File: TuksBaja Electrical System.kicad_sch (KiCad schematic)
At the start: 0 parts

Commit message: added two resistors to schematic
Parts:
- added R1, R2: R, symbol Device:R
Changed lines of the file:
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@@
 	(generator_version "9.0")
 	(paper "A4")
+	(symbol
+		(lib_id "Device:R")
+		(at 30.48 83.82 0)
+		(unit 1)
+		(exclude_from_sim no)
+		(in_bom yes)
+		(on_board yes)
+		(dnp no)
+		(fields_autoplaced yes)
+		(property "Reference" "R1"
+			(at 33.02 82.5499 0)
+			(effects
+				(font
+					(size 1.27 1.27)
+				)
+				(justify left)
+			)
+		)
+		(property "Value" "R"
+			(at 33.02 85.0899 0)
+			(effects
+				(font
+					(size 1.27 1.27)
+				)
+				(justify left)
+			)
+		)
+		(property "Footprint" ""
+			(at 28.702 83.82 90)
+			(effects
+				(font
+					(size 1.27 1.27)
+				)
+				(hide yes)
+			)
+		)
+		(property "Datasheet" "~"
+			(at 30.48 83.82 0)
+			(effects
+				(font
+					(size 1.27 1.27)
+				)
+				(hide yes)
+			)
+		)
+		(property "Description" "Resistor"
+			(at 30.48 83.82 0)
+			(effects
+				(font
+					(size 1.27 1.27)
+				)
+				(hide yes)
+			)
+		)
+		(pin "1"
+		)
+		(pin "2"
+		)
+		(instances
+			(project ""
+				(path "/32101482-20ad-4a29-9fb3-a9077501af62"
+					(reference "R1")
+					(unit 1)
+				)
+			)
+		)
+	)
+	(symbol
+		(lib_id "Device:R")
+		(at 30.48 105.41 0)
+		(unit 1)
+		(exclude_from_sim no)
+		(in_bom yes)
+		(on_board yes)
+		(dnp no)
+		(fields_autoplaced yes)
+		(property "Reference" "R2"
+			(at 33.02 104.1399 0)
+			(effects
+				(font
+					(size 1.27 1.27)
+				)
+				(justify left)
+			)
+		)
+		(property "Value" "R"
+			(at 33.02 106.6799 0)
+			(effects
+				(font
+					(size 1.27 1.27)
+				)
+				(justify left)
+			)
+		)
+		(property "Footprint" ""
+			(at 28.702 105.41 90)
+			(effects
+				(font
+					(size 1.27 1.27)
+				)
+				(hide yes)
+			)
+		)
+		(property "Datasheet" "~"
+			(at 30.48 105.41 0)
+			(effects
+				(font
+					(size 1.27 1.27)
+				)
+				(hide yes)
+			)
+		)
+		(property "Description" "Resistor"
+			(at 30.48 105.41 0)
+			(effects
+				(font
+					(size 1.27 1.27)
+				)
+				(hide yes)
+			)
+		)
+		(pin "2"
+		)
+		(pin "1"
+		)
+		(instances
+			(project ""
+				(path "/32101482-20ad-4a29-9fb3-a9077501af62"
+					(reference "R2")
+					(unit 1)
+				)
+			)
+		)
+	)
 	(sheet_instances
 		(path "/"

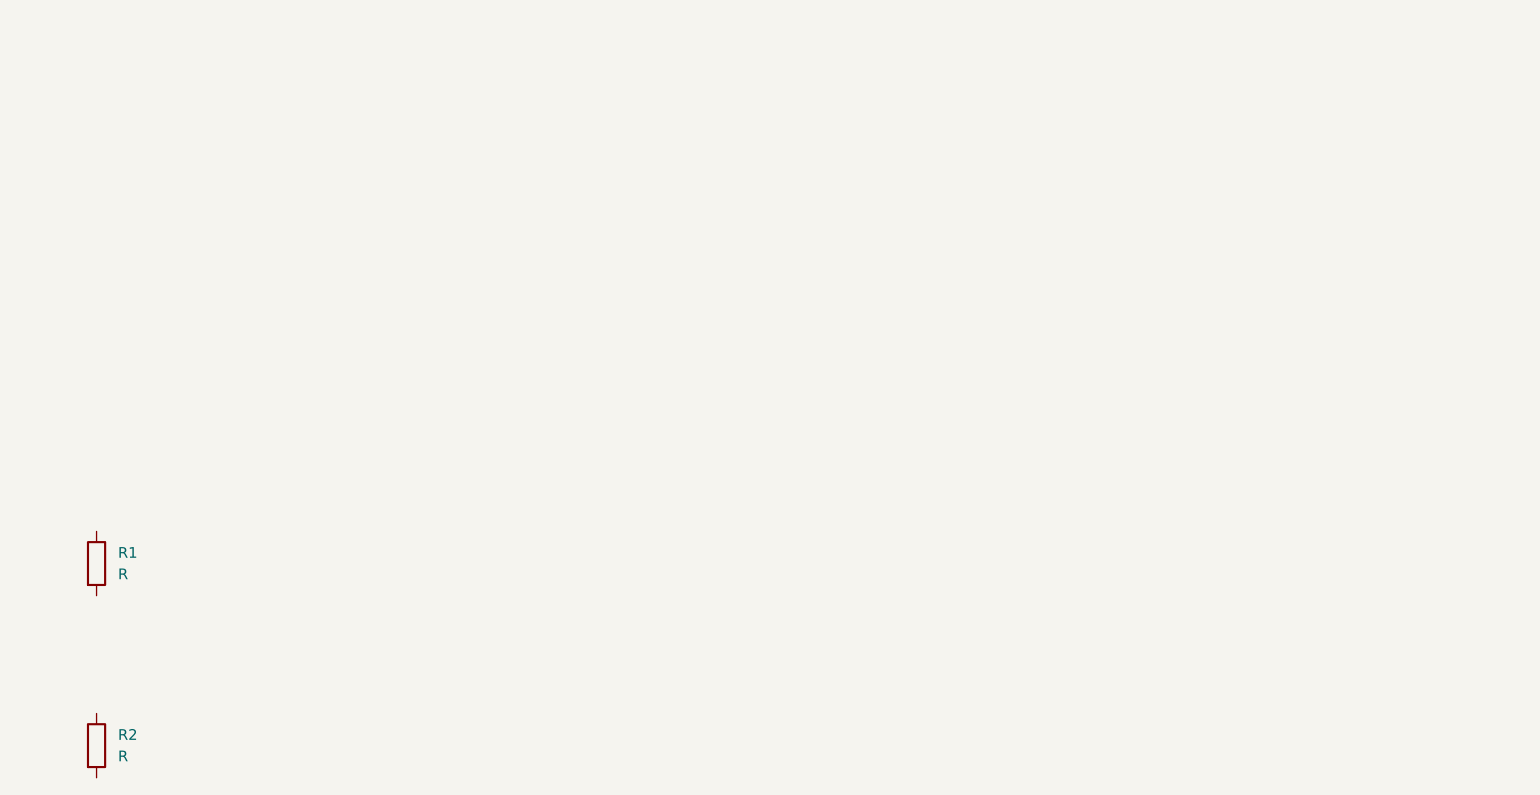
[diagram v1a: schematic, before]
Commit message: added arduino, buck converter, and battery
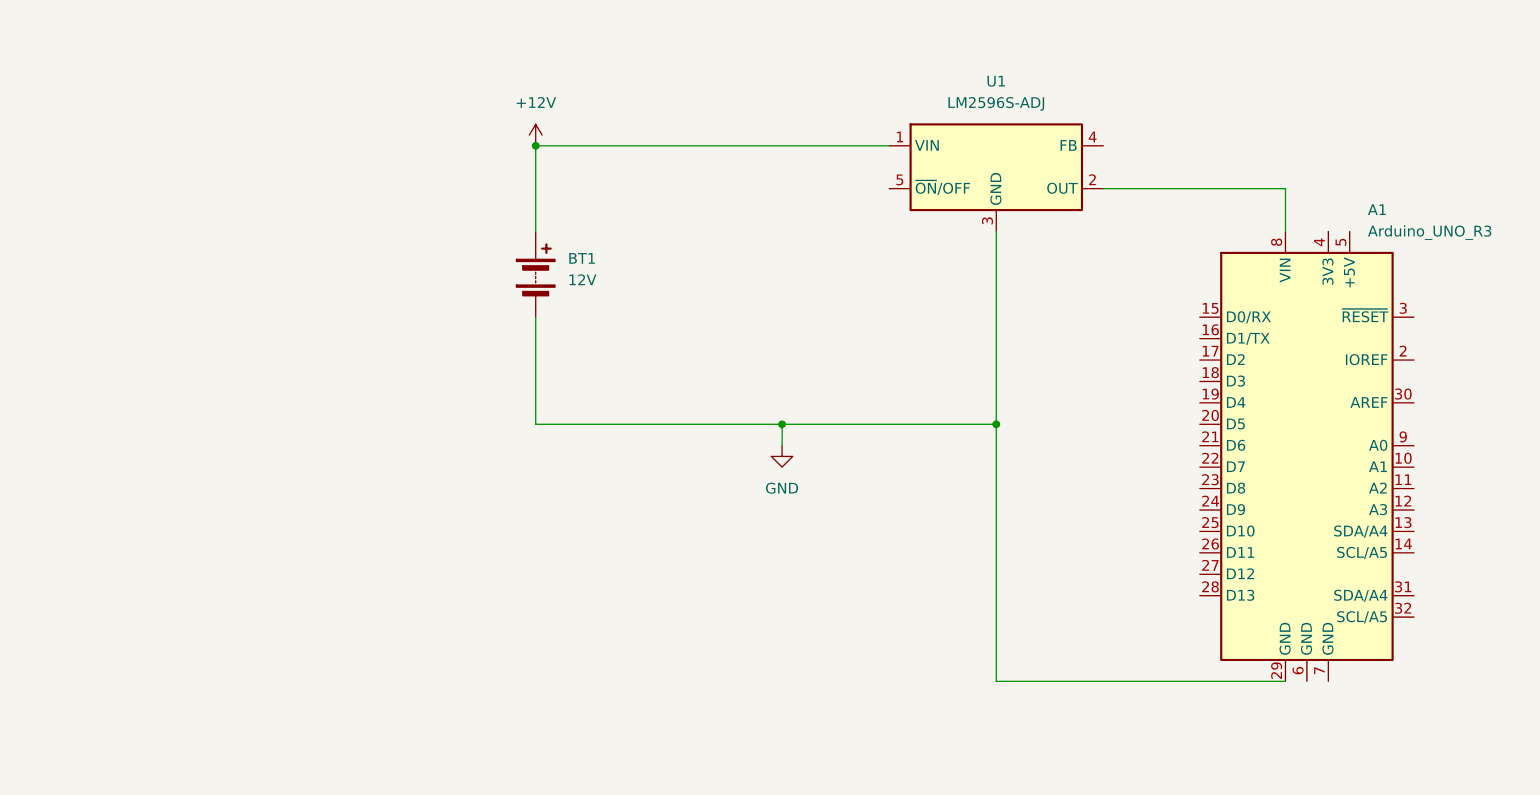
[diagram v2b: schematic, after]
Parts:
- removed R1, R2: R, symbol Device:R
- added A1: Arduino_UNO_R3, Module:Arduino_UNO_R3, symbol MCU_Module:Arduino_UNO_R3
- added BT1: 12V, symbol Device:Battery
- added U1: LM2596S-ADJ, Package_TO_SOT_SMD:TO-263-5_TabPin3, symbol Regulator_Switching:LM2596S-ADJ
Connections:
- new net: A1.8 (VIN), U1.2 (OUT)
- new net +12V: BT1.1 (+), U1.1 (VIN)
- new net GND: A1.29 (GND), BT1.2 (-), U1.3 (GND)

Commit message: completed power supply
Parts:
- removed A1: Arduino_UNO_R3, Module:Arduino_UNO_R3, symbol MCU_Module:Arduino_UNO_R3
- removed BT1: 12V, symbol Device:Battery
- added C_IN1: 470u, symbol Device:C
- added C_OUT1: 220u, symbol Device:C
- added D1: 1N5825, symbol Device:D_Schottky
- added L1: 68u, symbol Device:L
- added R1: 1k, symbol Device:R_US
- added R2: 3k, symbol Device:R_US
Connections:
- net +12V: now also C_IN1.1
- net GND: now also U1.5 (~{ON}/OFF), C_IN1.2, C_OUT1.2, D1.2 (A), R1.2
- net at U1.2 (OUT): now also D1.1 (K), L1.1
- net at U1.4 (FB): now also R1.1, R2.1
- new net +5V: C_OUT1.1, L1.2, R2.2
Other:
- note added: "Power Supply"
- company: (none) -> TuksBaja
- title: (none) -> Vehicle Electrical Schematic
